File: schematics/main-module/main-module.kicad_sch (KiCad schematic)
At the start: 131 parts, among them J1 Conn_01x02_Socket, J3 Conn_01x02_Pin, J3 USB_C_Receptacle_USB2.0, J4 Microphone, J5 Conn_01x04_Socket, J6 Conn_01x04_Pin, J7 Limit Switch, J8 Conn_01x02_Pin, J9 Charger port, M1 Creality 42-40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

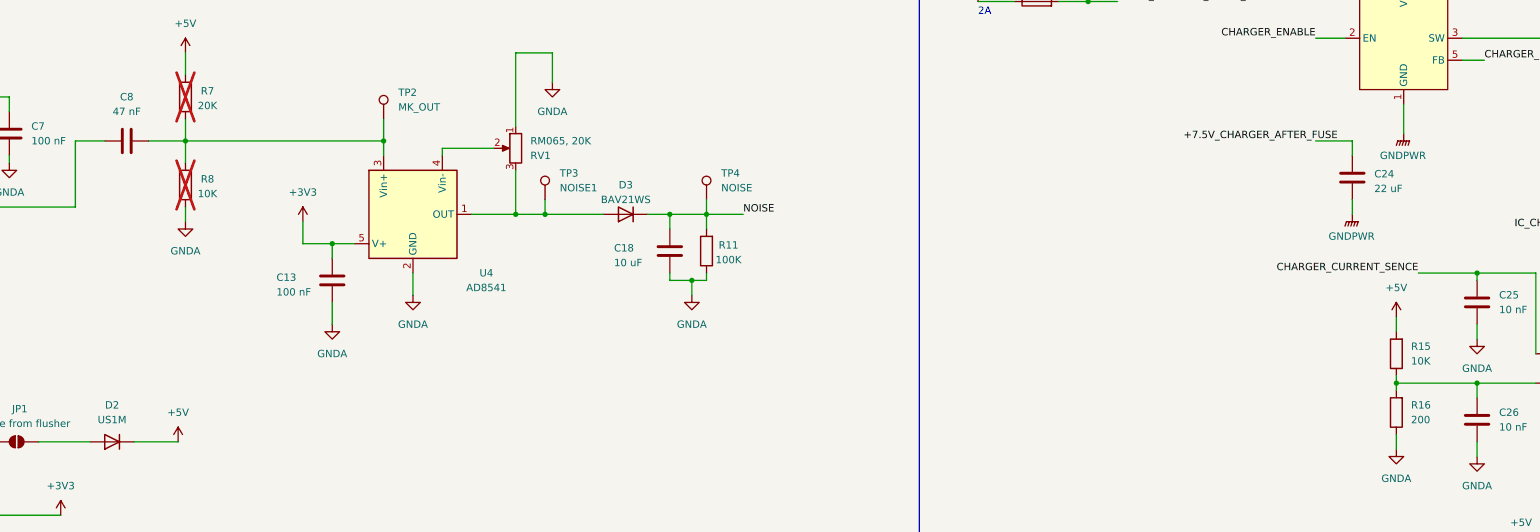
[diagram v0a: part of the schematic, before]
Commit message: charger (logic path) works normally
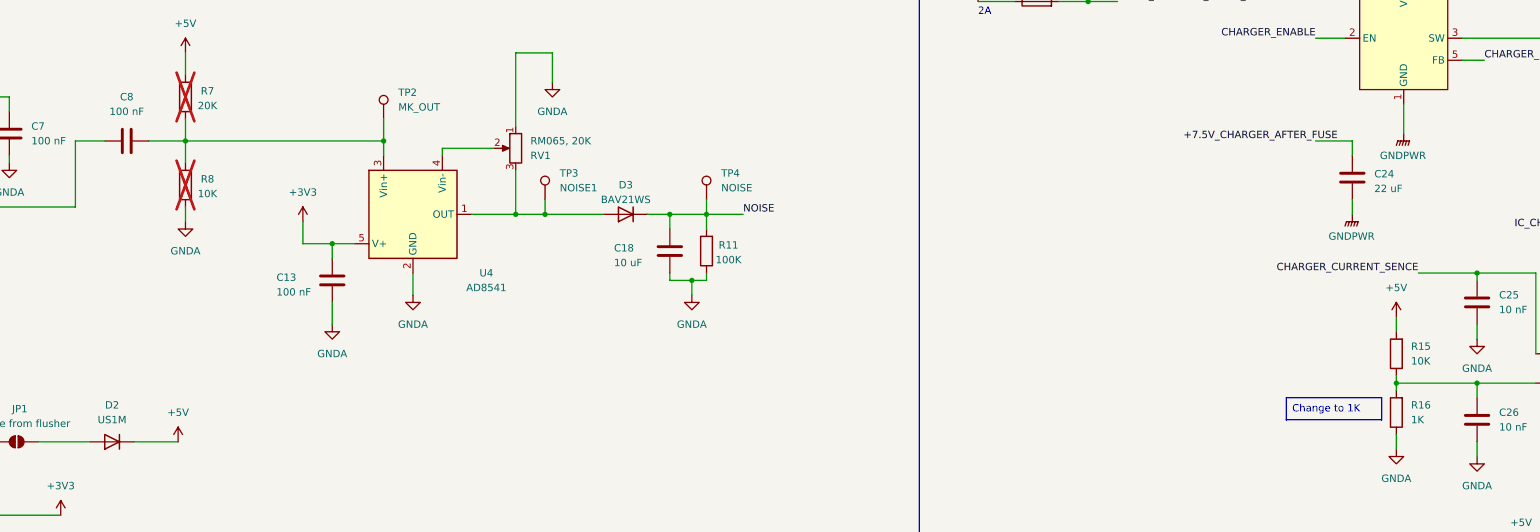
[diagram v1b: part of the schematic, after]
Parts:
- C8: value 47 nF -> 100 nF
- R16: value 200 -> 1K

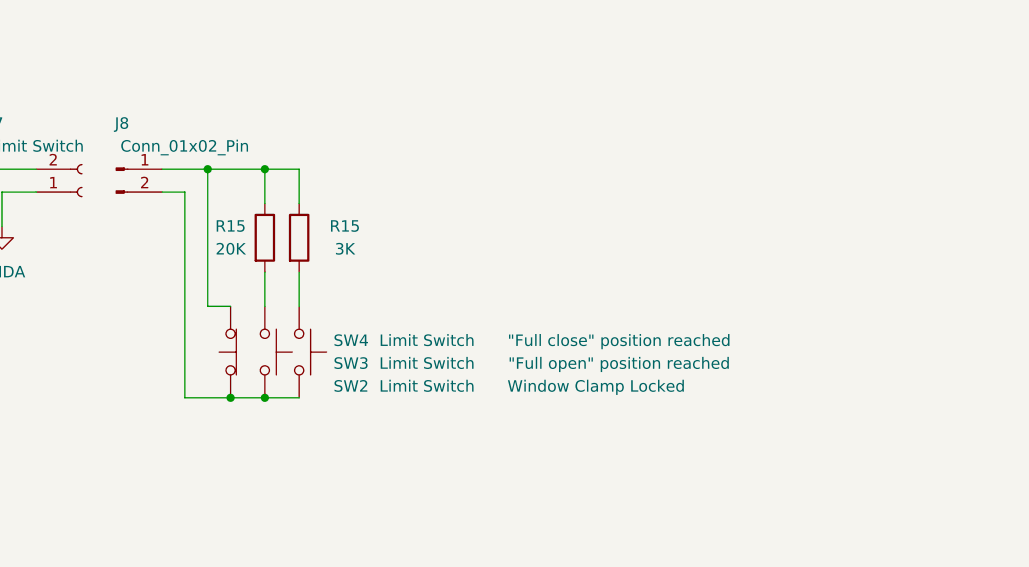
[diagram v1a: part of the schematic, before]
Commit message: added 'limit switch connected' logic
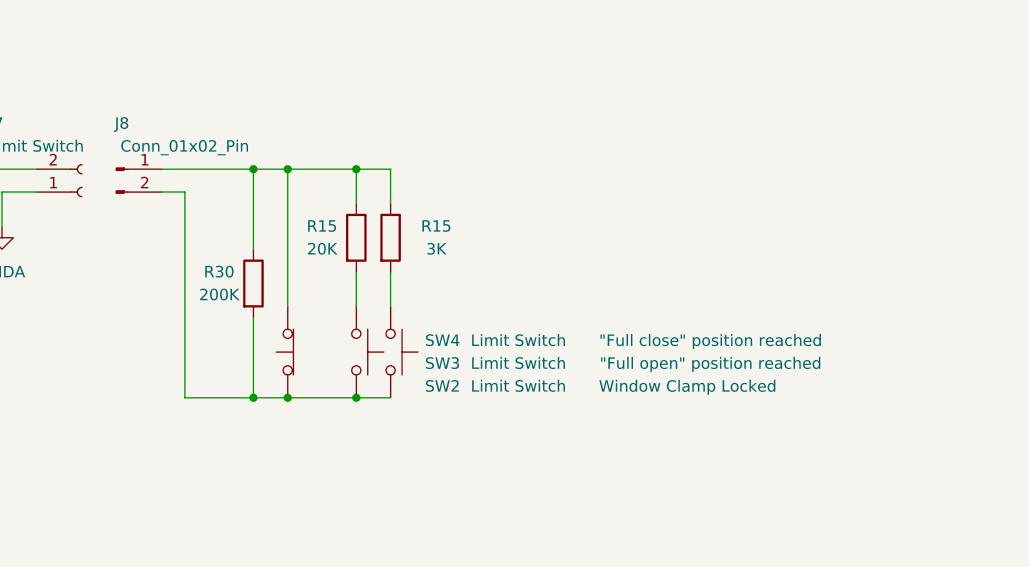
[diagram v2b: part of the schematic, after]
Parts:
- added R30: 200K, Resistor_SMD:R_0805_2012Metric, symbol Device:R
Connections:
- net at J8.2 (Pin_2), SW2.1 (A), SW3.2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: now also R30.2
- net at J8.1 (Pin_1), R15.1, R15.1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: now also R30.1
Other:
- moved on the sheet: R15, SW2, SW3, SW4

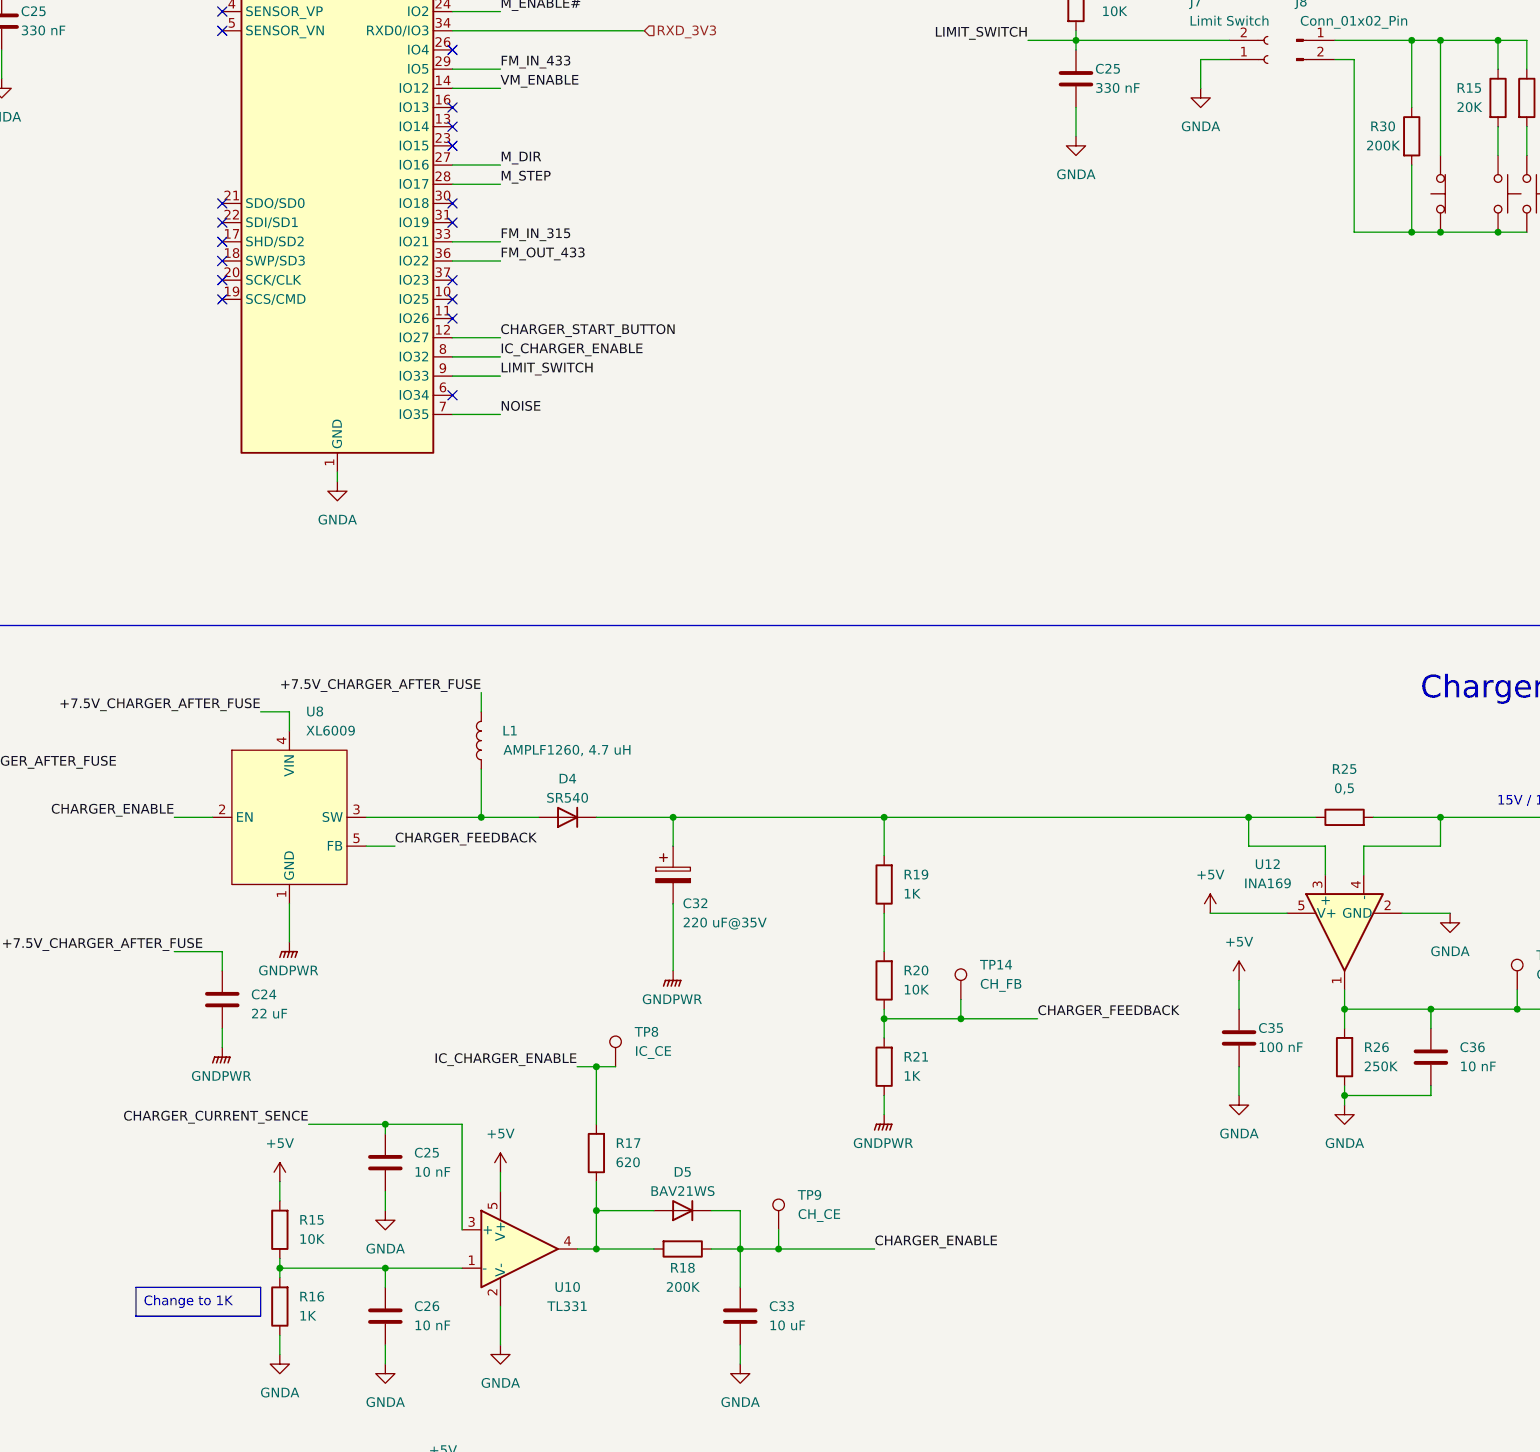
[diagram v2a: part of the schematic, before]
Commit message: noise alarm changes after hardware test
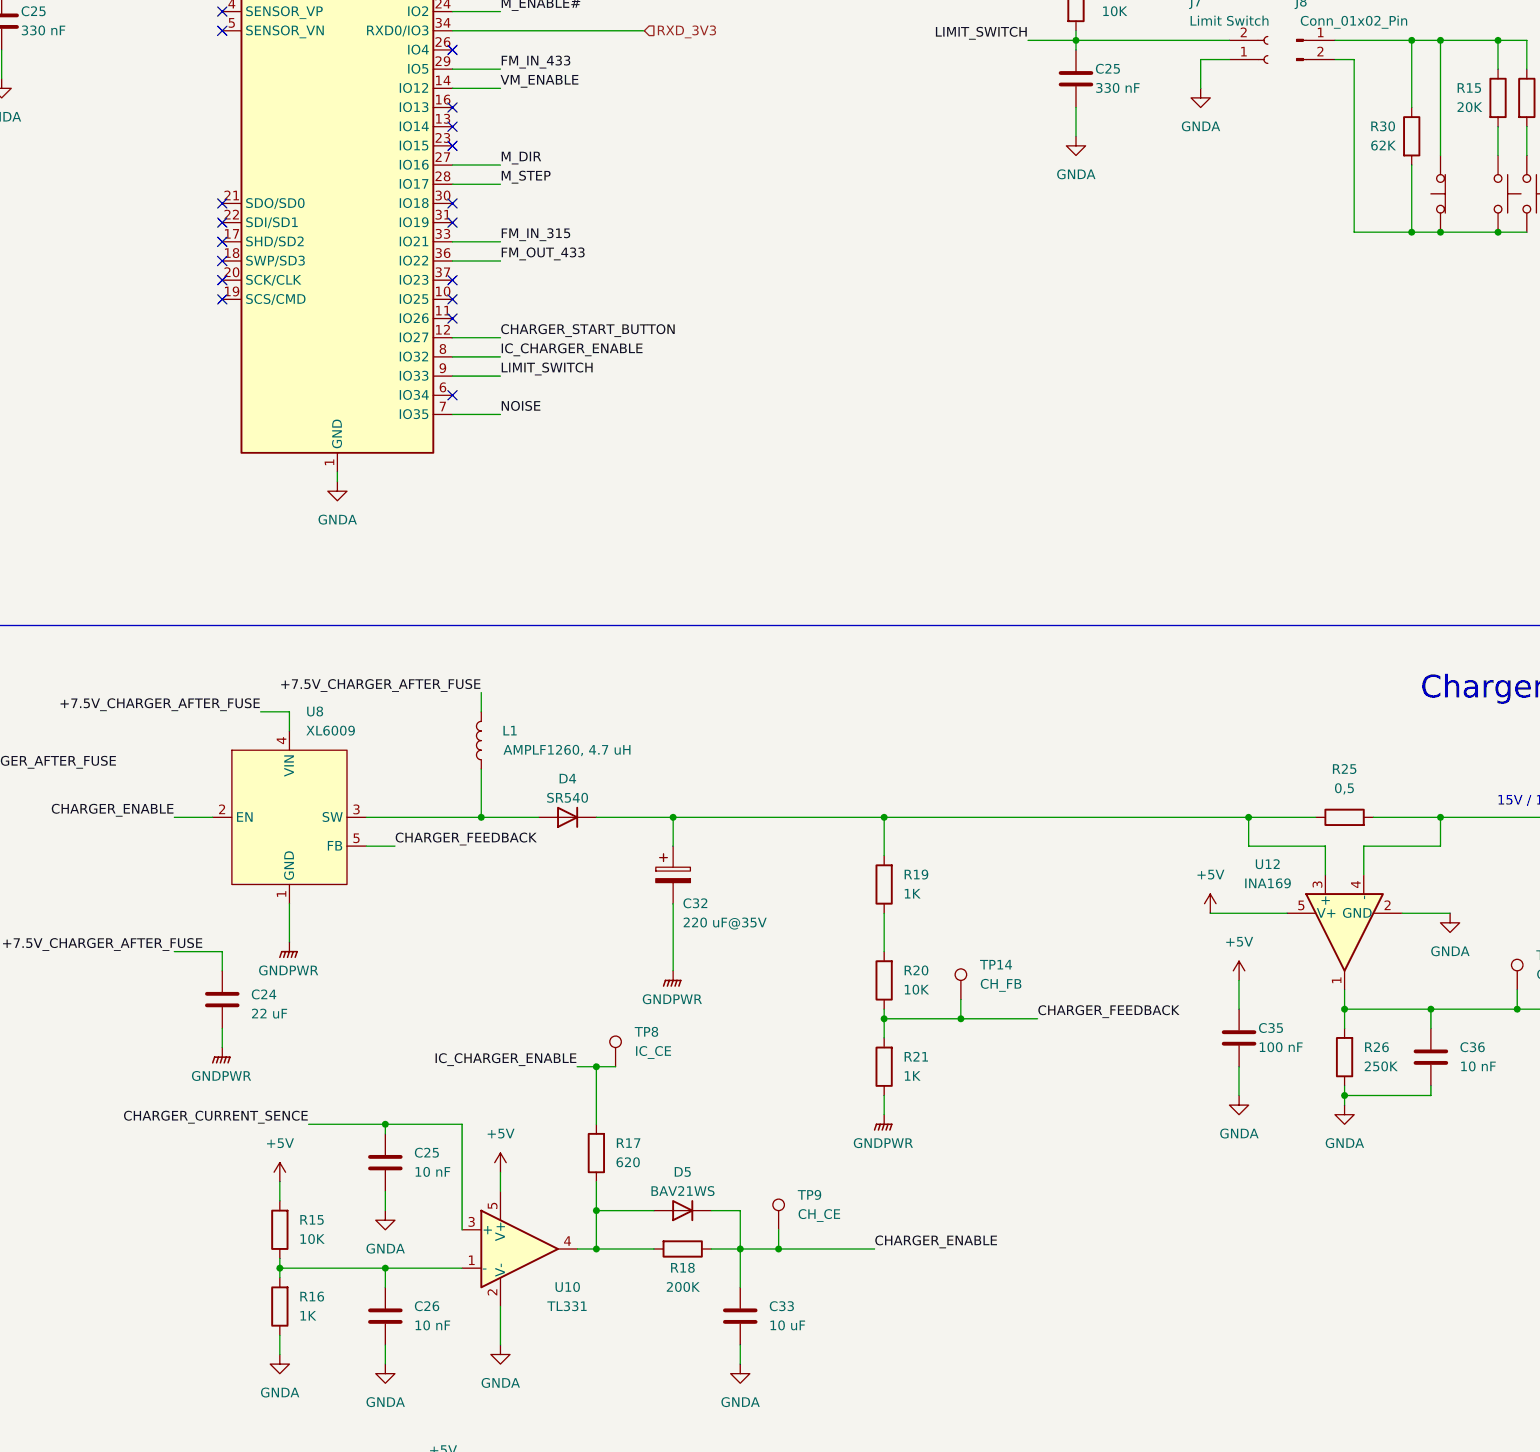
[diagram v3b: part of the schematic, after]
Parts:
- R30: value 200K -> 62K
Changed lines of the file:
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@@
 		)
 	)
-	(text_box "Change to 1K\n"
-		(exclude_from_sim no)
-		(at 317.5 267.97 0)
-		(size 16.51 3.81)
-		(stroke
-			(width 0)
-			(type default)
-		)
-		(fill
-			(type none)
-		)
-		(effects
-			(font
-				(size 1.27 1.27)
-			)
-			(justify left top)
-		)
-	)
 	(text "2A"
 		(exclude_from_sim no)
@@
 			)
 		)
-		(property "Value" "200K"
+		(property "Value" "62K"
 			(at 482.6 116.84 0)
 			(effects

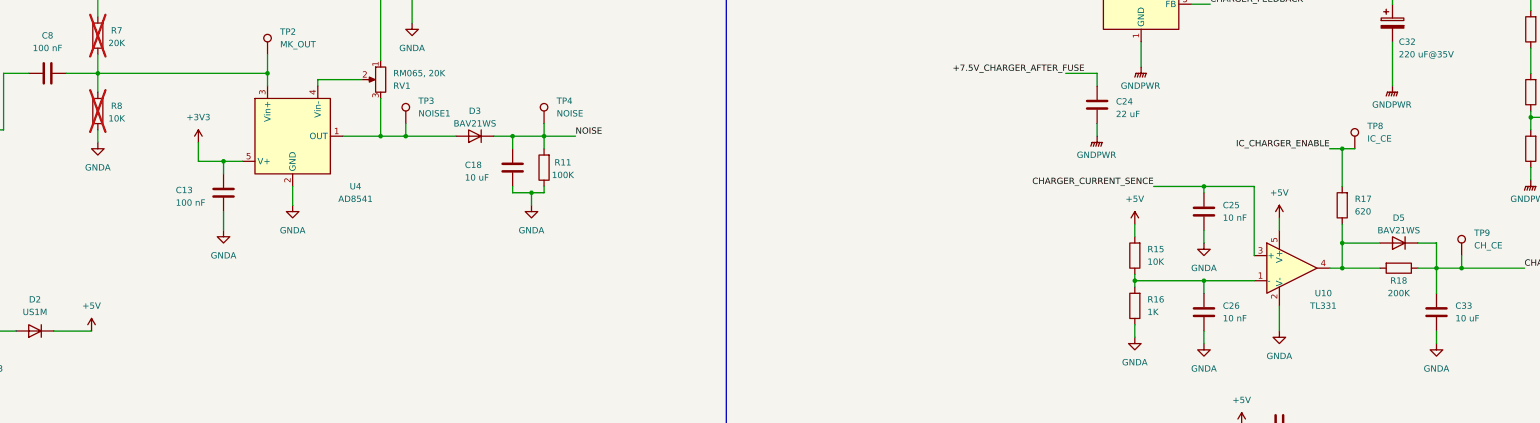
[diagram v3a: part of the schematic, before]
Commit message: handle module & main module almost done
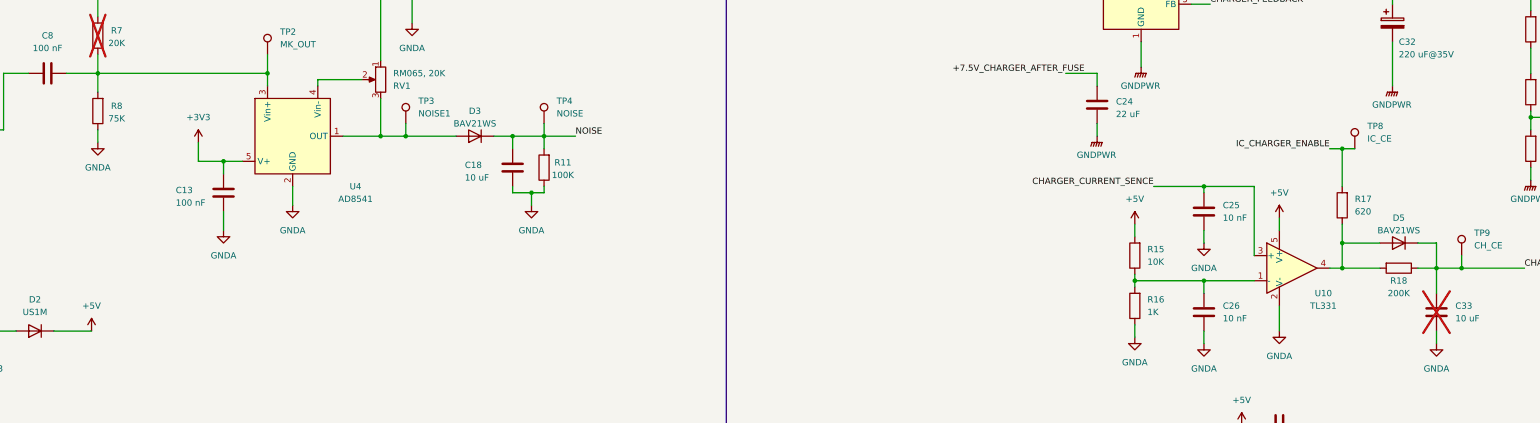
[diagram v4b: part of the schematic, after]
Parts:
- C33: now not fitted
- R8: value 10K -> 75K; now fitted
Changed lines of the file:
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@@
 		(in_bom yes)
 		(on_board yes)
-		(dnp no)
+		(dnp yes)
 		(property "Reference" "C33"
 			(at 401.32 270.51 0)
@@
 		(in_bom yes)
 		(on_board yes)
-		(dnp yes)
+		(dnp no)
 		(property "Reference" "R8"
 			(at 130.81 230.124 0)
@@
 			)
 		)
-		(property "Value" "10K"
+		(property "Value" "75K"
 			(at 130.81 232.664 0)
 			(effects

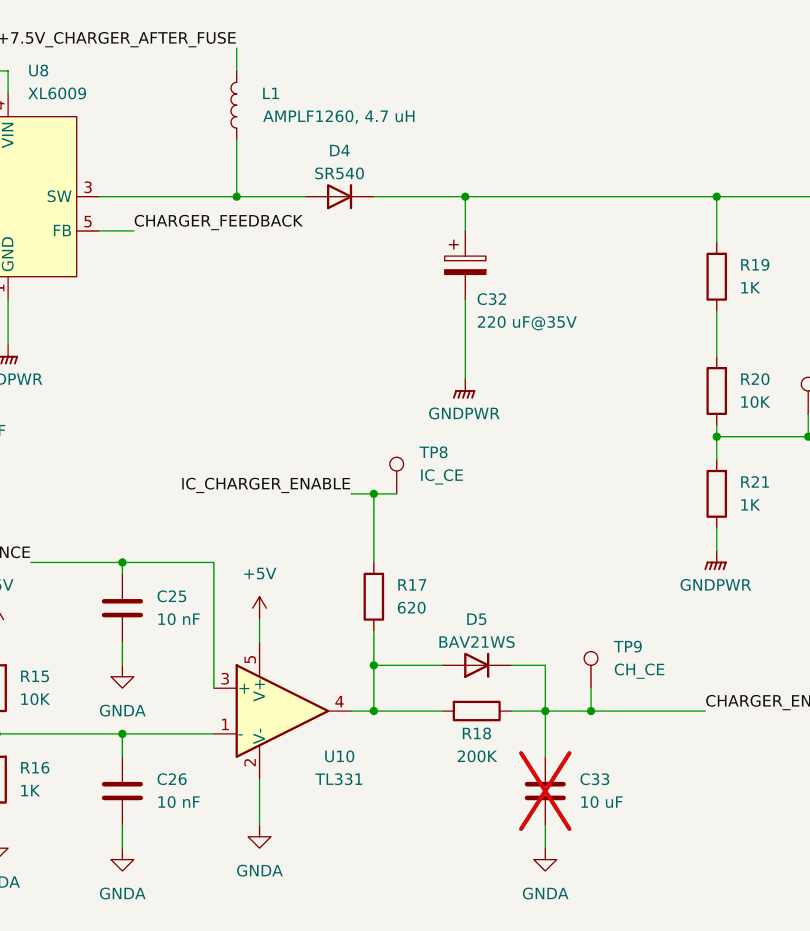
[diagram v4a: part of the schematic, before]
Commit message: i found problems with 315MHZ freq (some transmitter blocks air near me). So I added another remote control and I will create box for it
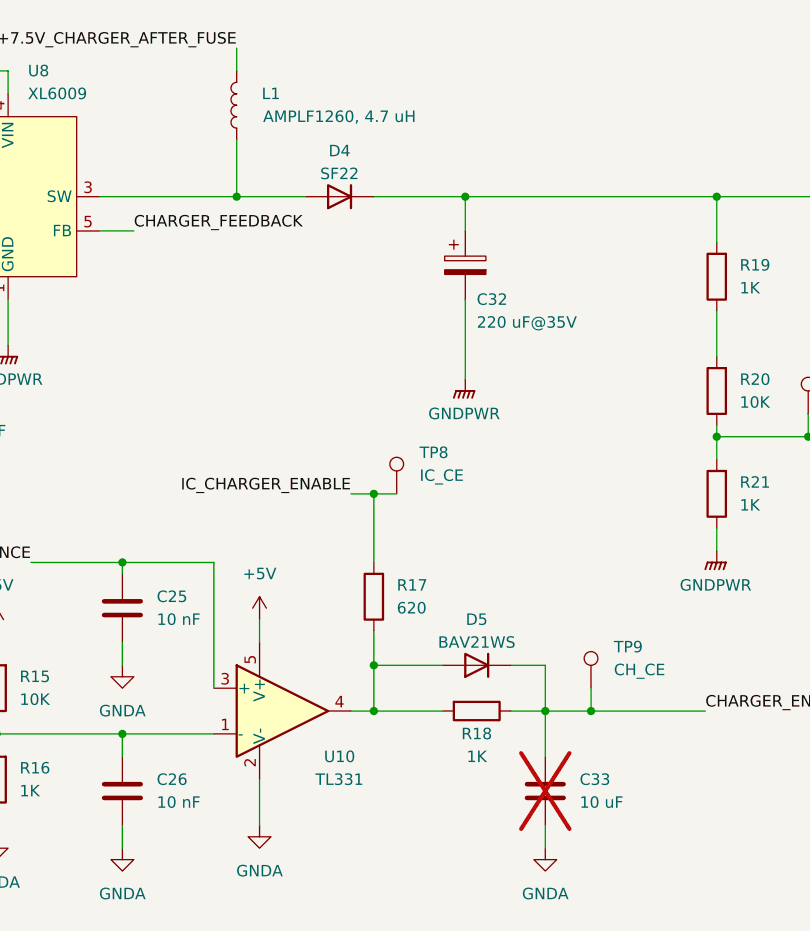
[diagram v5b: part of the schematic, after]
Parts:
- D4: value SR540 -> SF22
- R18: value 200K -> 1K
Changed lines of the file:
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@@
 			)
 		)
-		(property "Value" "200K"
+		(property "Value" "1K"
 			(at 389.89 267.97 90)
 			(effects
@@
 			)
 		)
-		(property "Value" "SR540"
+		(property "Value" "SF22"
 			(at 374.65 203.2 0)
 			(effects
